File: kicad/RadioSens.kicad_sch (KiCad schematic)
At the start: 8 parts, among them U1 12V, U2 12V, U3 12V

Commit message: Add voltage value to caps, update BOM, SCH, ASM
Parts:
- R1, R2, R3: Case/Package 0000 -> 0603; Tolerance ±% -> ±5%
- U1, U2, U3: now left out of the parts list

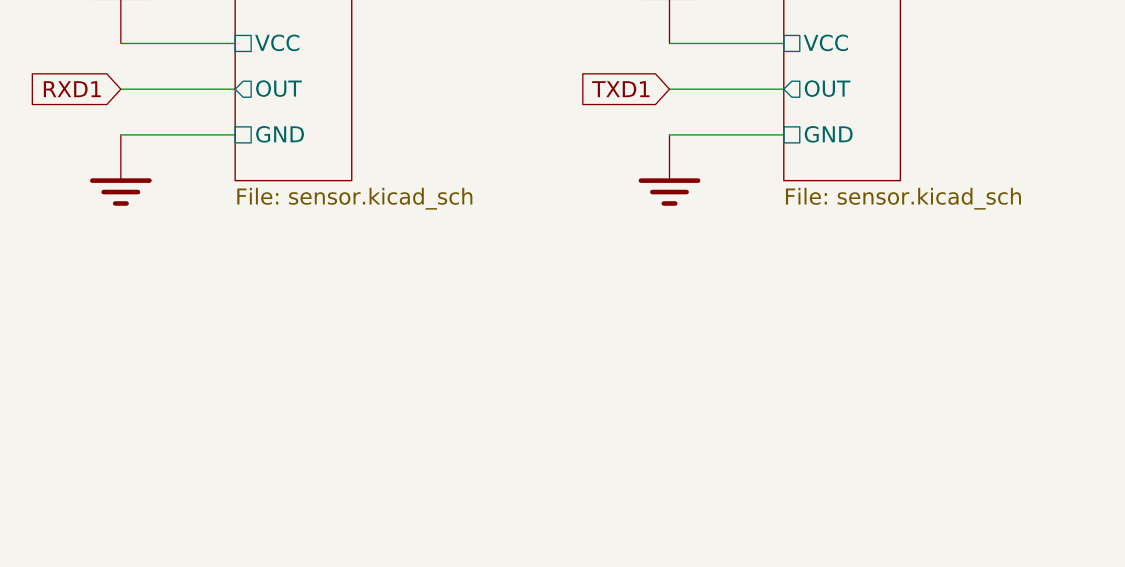
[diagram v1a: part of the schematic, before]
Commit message: Add docs; Update values of components according to PCB
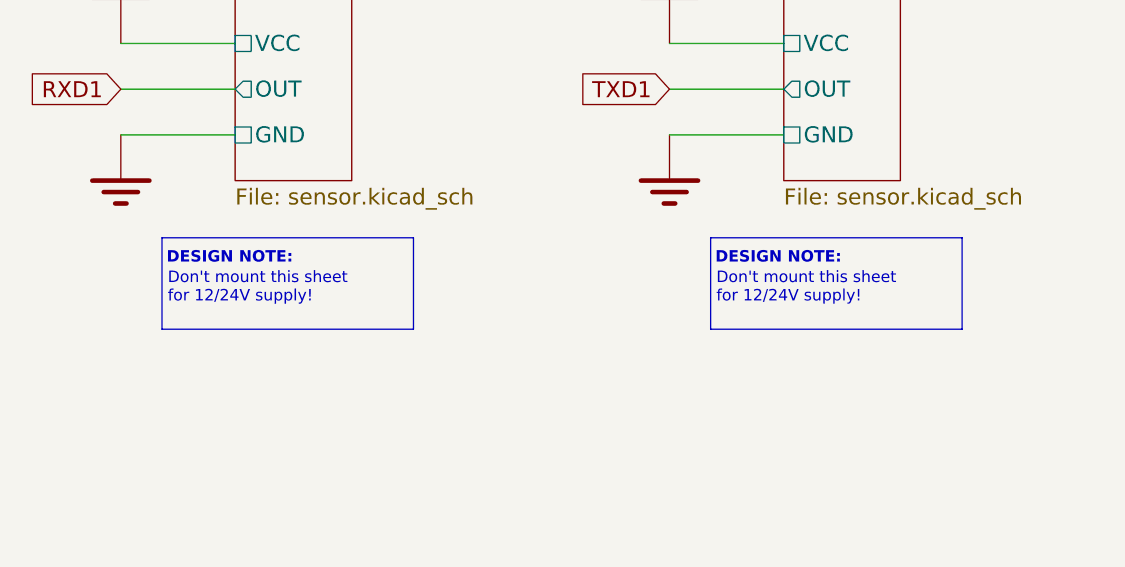
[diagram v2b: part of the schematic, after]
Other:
- note added: "Don't mount this sheet for 12/24V supply!"
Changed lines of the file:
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@@
     (stroke (width 0) (type default) (color 0 0 0 0))
+  )
+  (polyline (pts (xy 340.36 205.74) (xy 340.36 215.9))
+    (stroke (width 0) (type default) (color 0 132 132 1))
   )
   (polyline (pts (xy 326.136 349.25) (xy 354.33 349.25))
@@
     (stroke (width 0) (type default) (color 0 0 0 0))
   )
+  (polyline (pts (xy 251.46 205.74) (xy 279.4 205.74))
+    (stroke (width 0) (type default) (color 0 132 132 1))
+  )
   (wire (pts (xy 261.874 290.576) (xy 261.874 285.496))
     (stroke (width 0) (type default) (color 0 0 0 0))
@@
     (stroke (width 0) (type default) (color 0 0 0 0))
   )
+  (polyline (pts (xy 279.4 205.74) (xy 279.4 215.9))
+    (stroke (width 0) (type default) (color 0 132 132 1))
+  )
   (wire (pts (xy 241.3 335.026) (xy 248.92 335.026))
     (stroke (width 0) (type default) (color 0 0 0 0))
@@
     (stroke (width 0) (type default) (color 0 132 132 1))
   )
+  (polyline (pts (xy 312.42 205.74) (xy 312.42 215.9))
+    (stroke (width 0) (type default) (color 0 132 132 1))
+  )
+  (polyline (pts (xy 340.36 215.9) (xy 312.42 215.9))
+    (stroke (width 0) (type default) (color 0 132 132 1))
+  )
   (wire (pts (xy 413.512 65.786) (xy 416.052 65.786))
     (stroke (width 0) (type default) (color 0 0 0 0))
@@
     (stroke (width 0) (type default) (color 0 0 0 0))
   )
+  (polyline (pts (xy 312.42 205.74) (xy 340.36 205.74))
+    (stroke (width 0) (type default) (color 0 132 132 1))
+  )
   (wire (pts (xy 482.6 156.972) (xy 485.14 156.972))
     (stroke (width 0) (type default) (color 0 0 0 0))
@@
   (wire (pts (xy 62.738 89.408) (xy 65.278 89.408))
     (stroke (width 0) (type default) (color 0 0 0 0))
+  )
+  (polyline (pts (xy 251.46 205.74) (xy 251.46 215.9))
+    (stroke (width 0) (type default) (color 0 132 132 1))
   )
   (wire (pts (xy 62.738 58.928) (xy 65.278 58.928))
@@
     (stroke (width 0) (type default) (color 0 0 0 0))
   )
+  (polyline (pts (xy 279.4 215.9) (xy 251.46 215.9))
+    (stroke (width 0) (type default) (color 0 132 132 1))
+  )
   (wire (pts (xy 298.45 73.914) (xy 300.99 73.914))
     (stroke (width 0) (type default) (color 0 0 0 0))
@@
     (effects (font (size 5.0038 5.0038) (thickness 1.0008) bold italic) (justify left bottom))
   )
+  (text "Don't mount this sheet\nfor 12/24V supply!" (at 252.095 213.106 0)
+    (effects (font (size 1.27 1.27)) (justify left bottom))
+  )
   (text "Voltage Regulator 3.0V" (at 321.9449 314.579 0)
     (effects (font (size 5.0038 5.0038) (thickness 1.0008) bold italic) (justify left bottom))
   )
+  (text "DESIGN NOTE:" (at 251.968 208.788 0)
+    (effects (font (size 1.27 1.27) (thickness 0.254) bold) (justify left bottom))
+  )
   (text "DESIGN NOTE:" (at 326.644 352.298 0)
     (effects (font (size 1.27 1.27) (thickness 0.254) bold) (justify left bottom))
@@
     (effects (font (size 5.0038 5.0038) (thickness 1.0008) bold italic) (justify left bottom))
   )
+  (text "DESIGN NOTE:" (at 312.928 208.788 0)
+    (effects (font (size 1.27 1.27) (thickness 0.254) bold) (justify left bottom))
+  )
   (text "Hall Sensor 2" (at 294.132 172.212 0)
     (effects (font (size 5.0038 5.0038) (thickness 1.0008) bold italic) (justify left bottom))
@@
   (text "RS485" (at 355.727 257.937 0)
     (effects (font (size 5.0038 5.0038) (thickness 1.0008) bold italic) (justify left bottom))
+  )
+  (text "Don't mount this sheet\nfor 12/24V supply!" (at 313.055 213.106 0)
+    (effects (font (size 1.27 1.27)) (justify left bottom))
   )
   (text "Additional Feature" (at 259.334 156.21 0)
@@
     )
     (path "/a4b9bbb0-bcb1-4d37-9cab-9a934c822991/8055e129-dfa8-42a4-b9af-f731e2009a97"
-      (reference "C26") (unit 1) (value "22u/50V") (footprint "Capacitor_SMD:CP_Elec_8x6.5")
+      (reference "C26") (unit 1) (value "47u/50V") (footprint "Capacitor_SMD:CP_Elec_8x6.5")
     )
     (path "/a4b9bbb0-bcb1-4d37-9cab-9a934c822991/521ddfe3-6ea1-47dc-bd6a-d24c716a1a20"
-      (reference "C27") (unit 1) (value "22u/50V") (footprint "Capacitor_SMD:CP_Elec_8x6.5")
+      (reference "C27") (unit 1) (value "47u/50V") (footprint "Capacitor_SMD:CP_Elec_8x6.5")
     )
     (path "/a4b9bbb0-bcb1-4d37-9cab-9a934c822991/62d306ff-29c9-4bc1-bf35-3250fd55bf67"
@@
     )
     (path "/0d05d38b-5bdf-4eb7-beb0-3870a403aaf7/db4832f1-bb89-4ddd-af57-0fca5e8d1261"
-      (reference "C38") (unit 1) (value "4.7u/25V") (footprint "Capacitor_SMD:C_0603_1608Metric")
+      (reference "C38") (unit 1) (value "4.7u/6.3V") (footprint "Capacitor_SMD:C_0603_1608Metric")
     )
     (path "/0d05d38b-5bdf-4eb7-beb0-3870a403aaf7/271fa1f8-4094-4c83-b40b-122d9748320d"

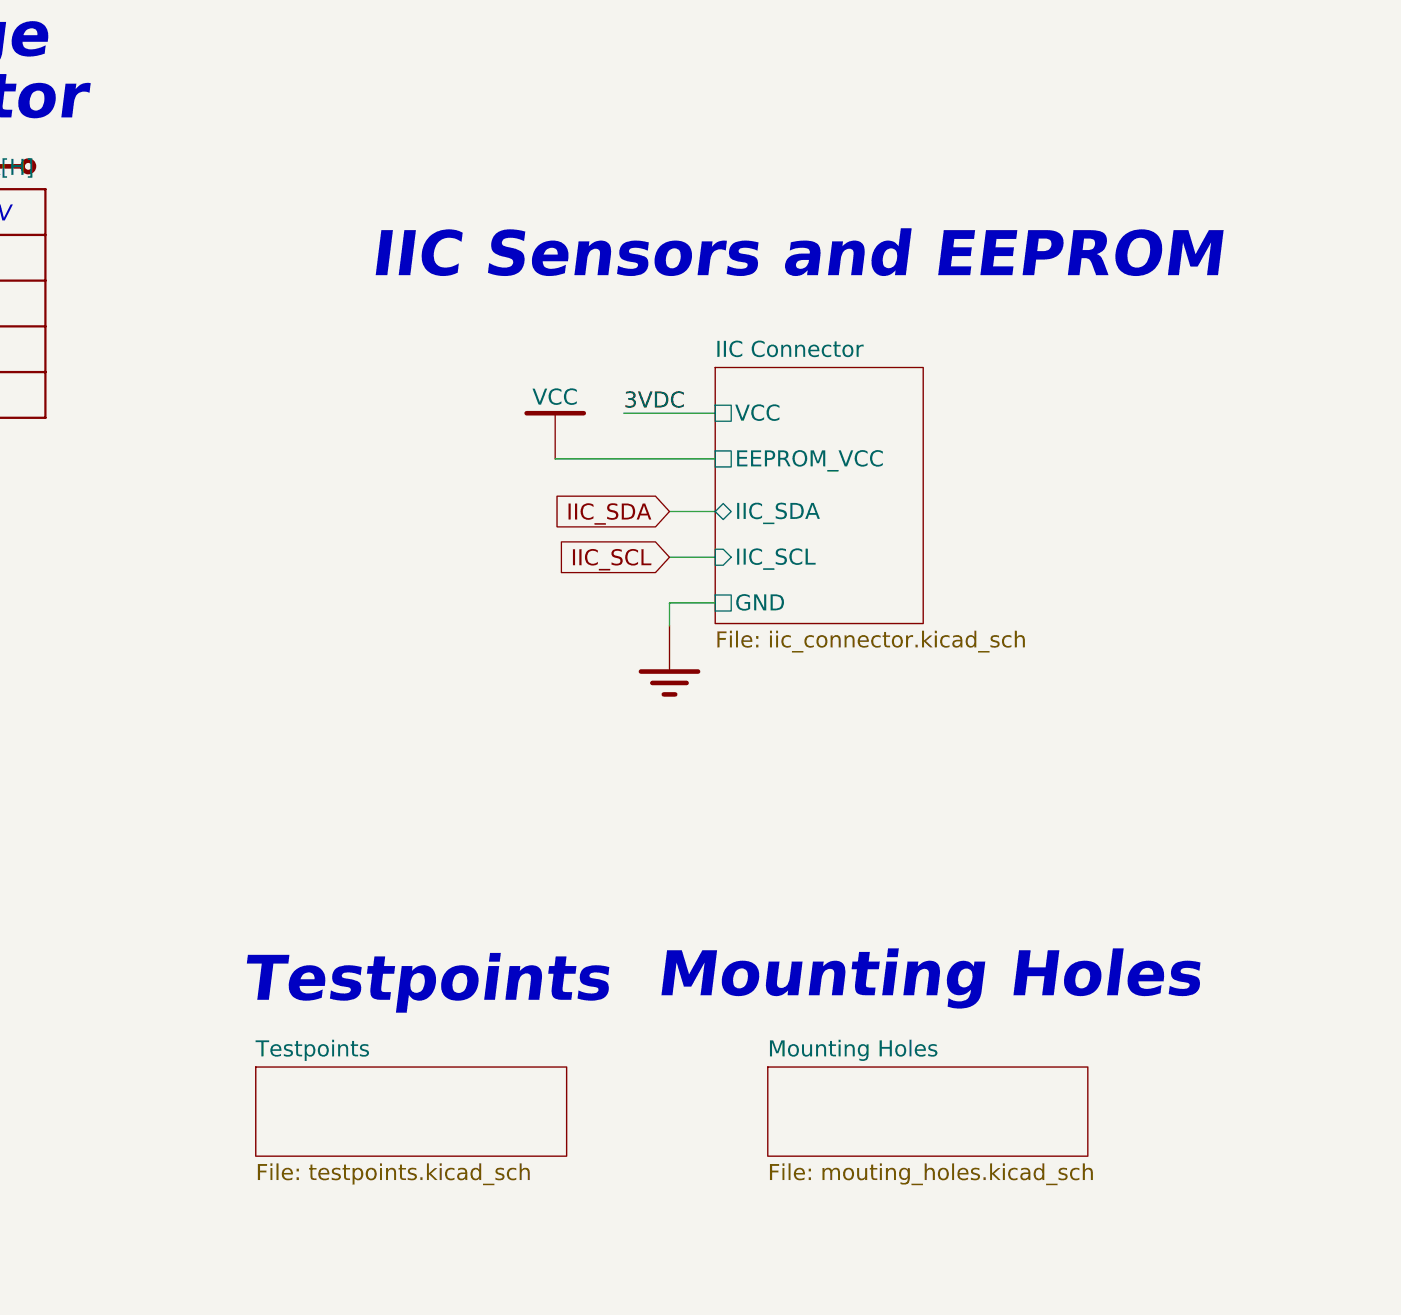
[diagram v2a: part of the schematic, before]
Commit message: Add wiring diagram; Add work ours (stage 2); refactor folders
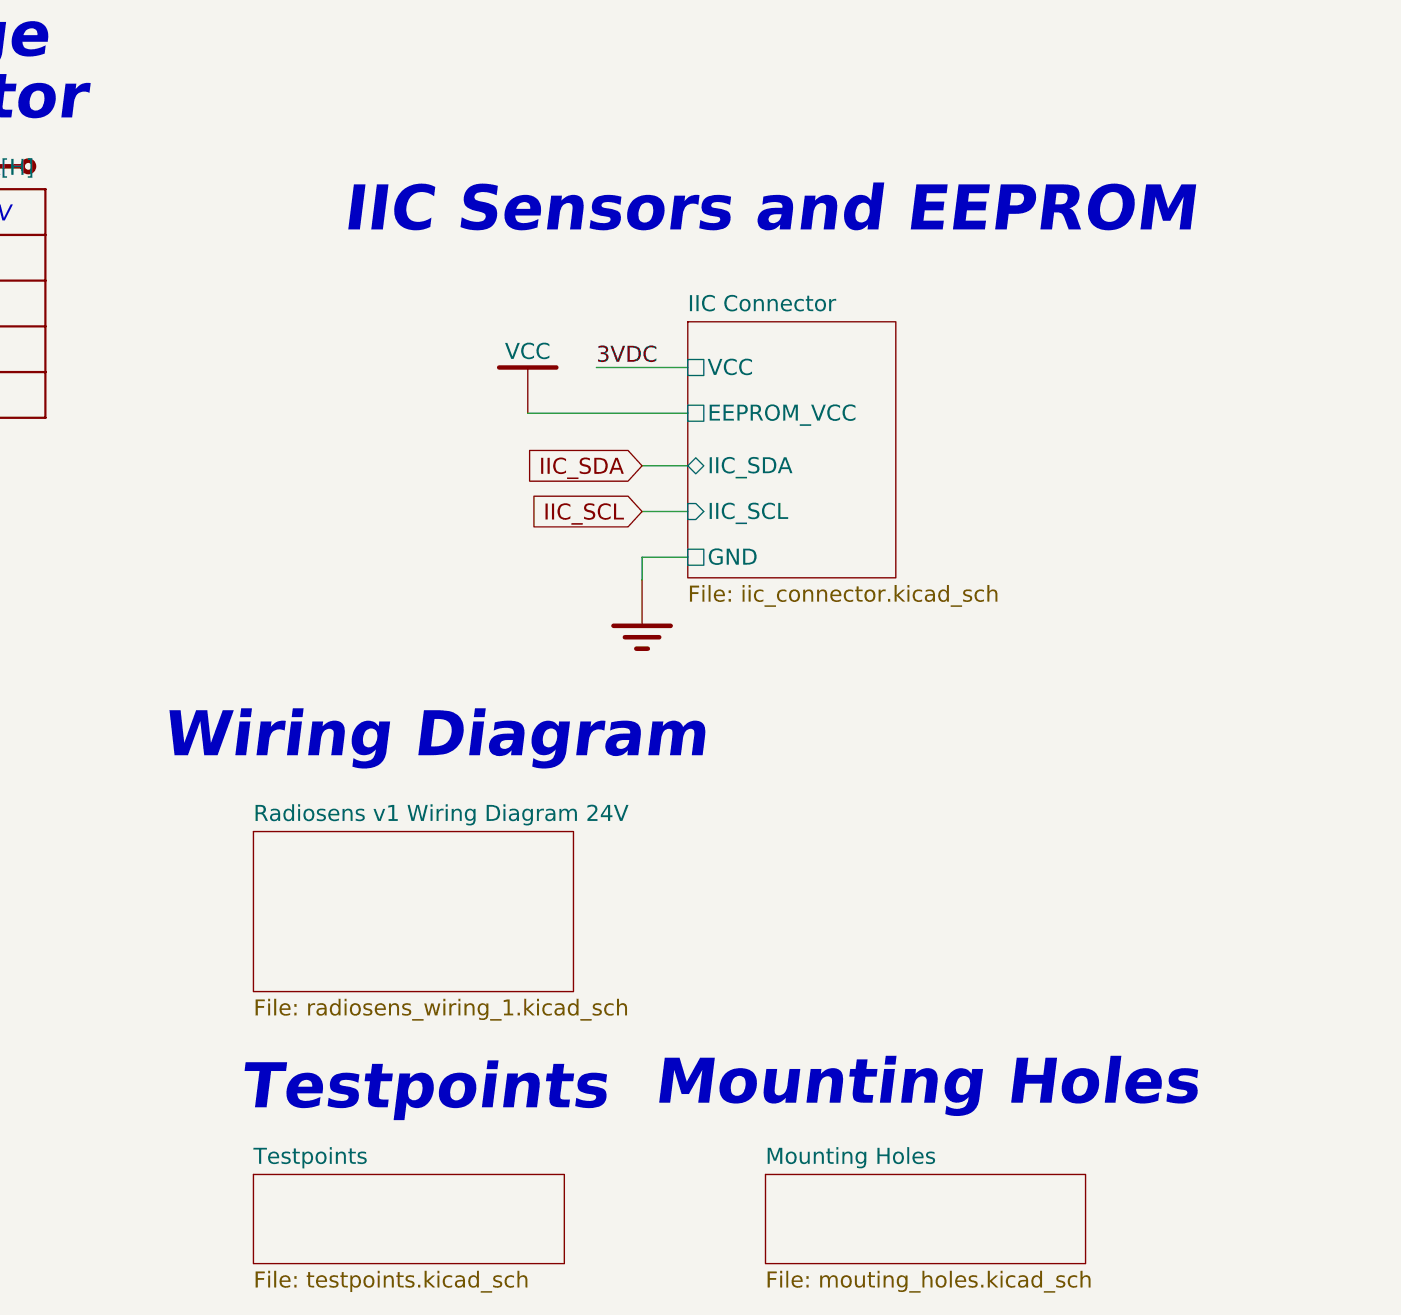
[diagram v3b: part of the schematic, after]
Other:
- added sheet Radiosens v1 Wiring Diagram 24V (radiosens_wiring_1.kicad_sch)
- note added: "Wiring Diagram"
- title: Remote Sensor -> RadioSens v1

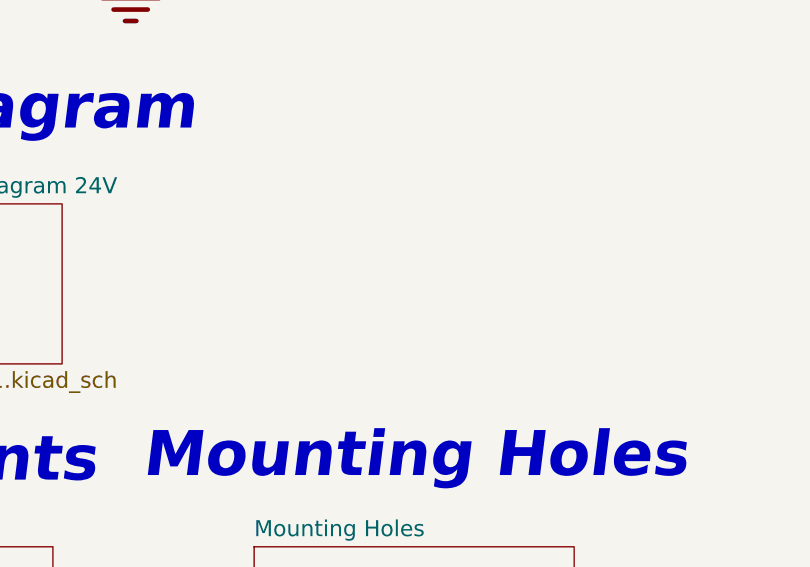
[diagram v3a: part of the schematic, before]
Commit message: update: to 7.0 ver and add fiducials
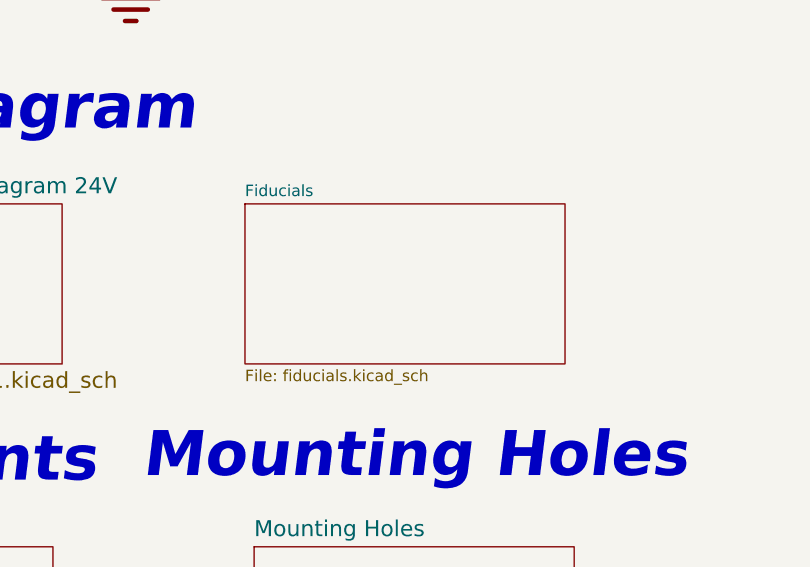
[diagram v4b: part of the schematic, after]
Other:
- added sheet Fiducials (fiducials.kicad_sch)
